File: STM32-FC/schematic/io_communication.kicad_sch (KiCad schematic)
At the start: 17 parts, among them J11 GH 1.25mm 6P, J12 GH 1.25mm 6P, J13 GH 1.25mm 4P, J14 GH 1.25mm 4P, J15 GH 1.25mm 4P, U10 ATA6561-GBQW, U11 ATA6561-GBQW

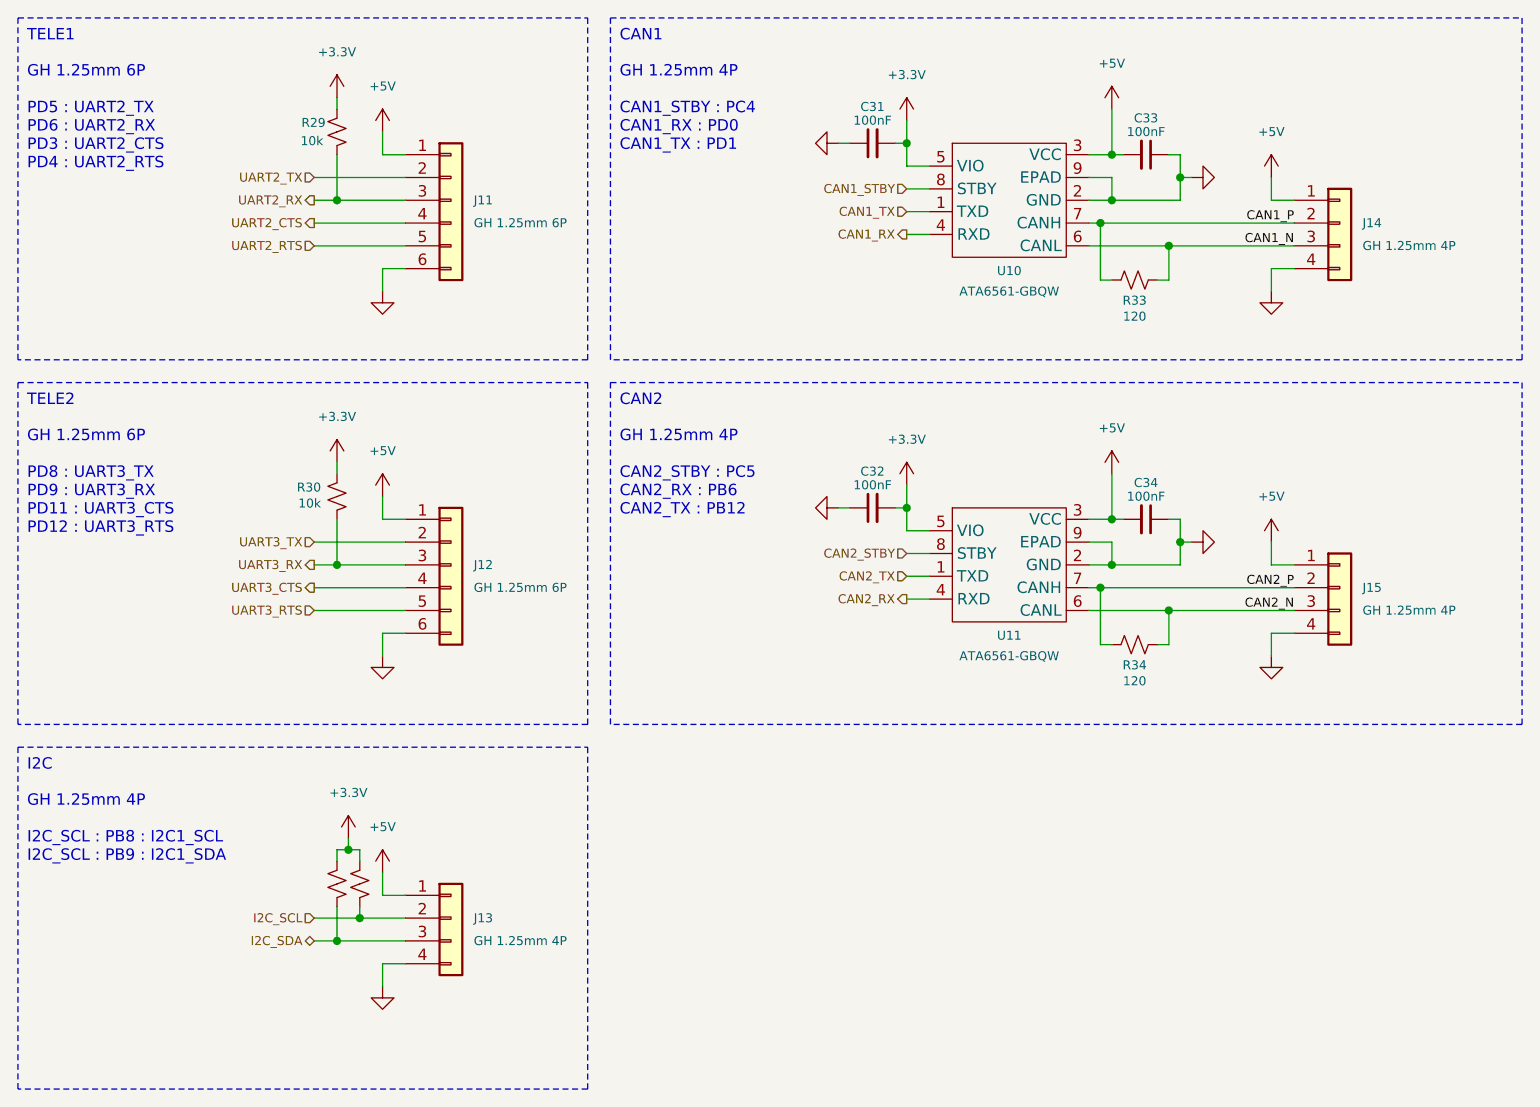
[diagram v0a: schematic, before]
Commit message: schematic update
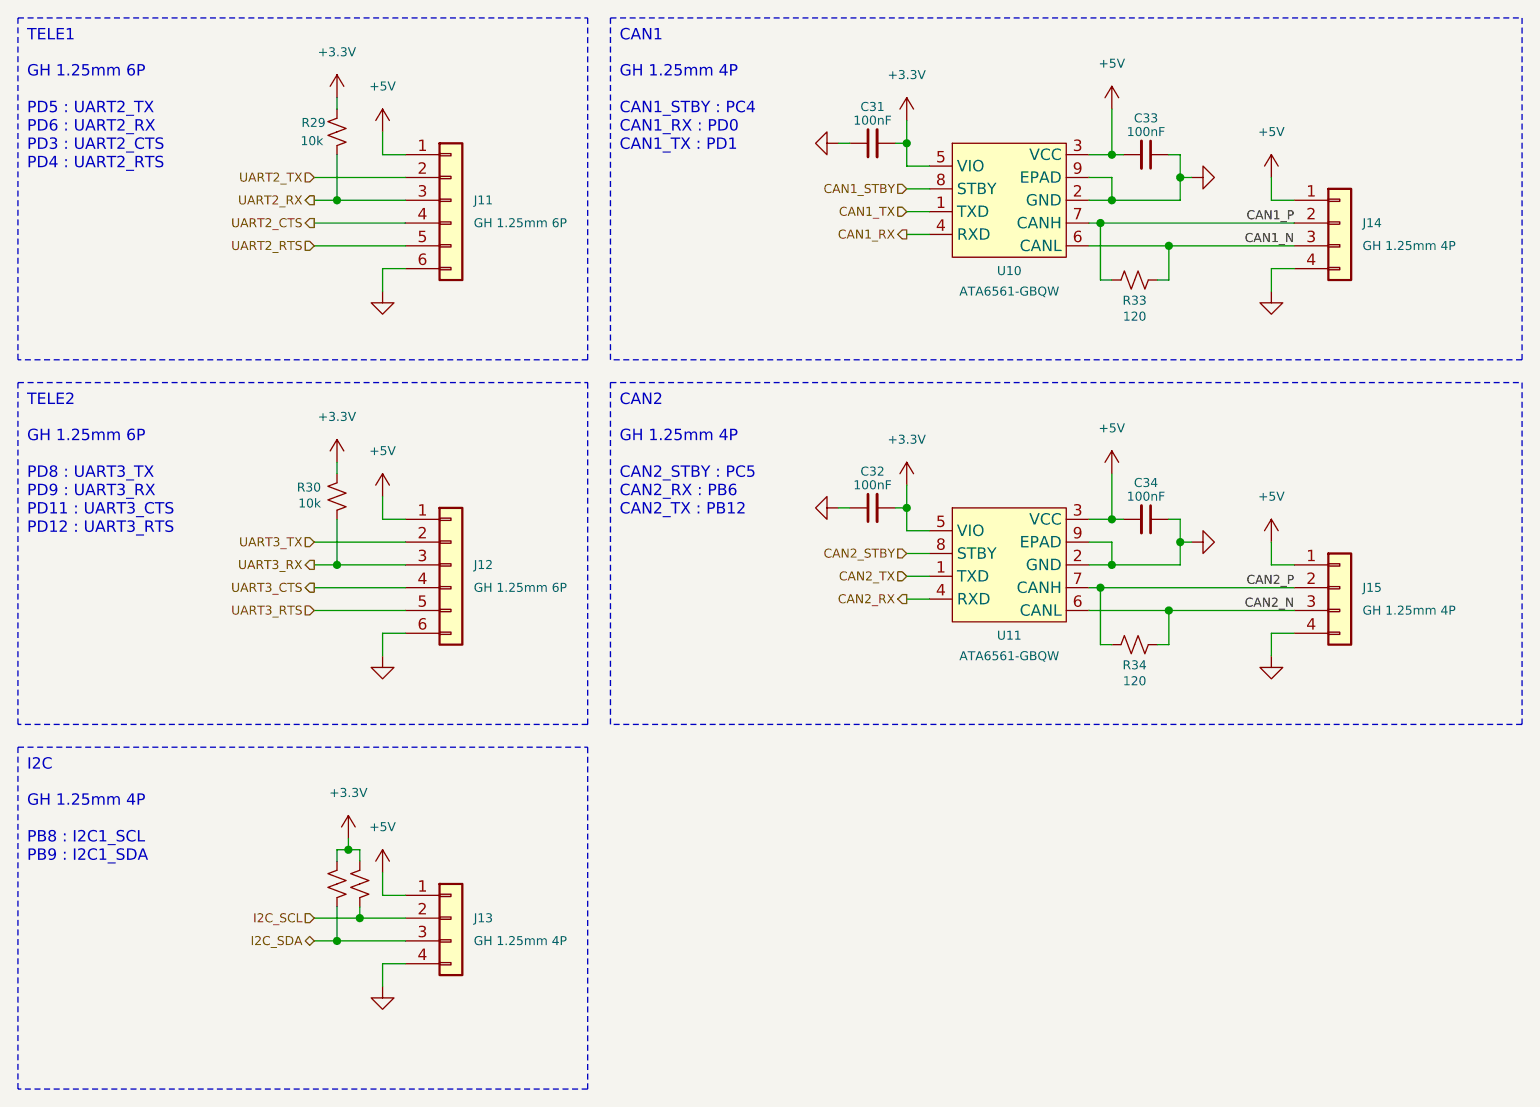
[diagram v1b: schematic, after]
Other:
- note added: "GH 1.25mm 4P PB8 : I2C1_SCL PB9 : I2C1_SDA"
- note removed: "GH 1.25mm 4P I2C_SCL : PB8 : I2C1_SCL I2C_SCL : PB9 : I2C1_SDA"
- title: Communication -> STM32 Flight Controller
